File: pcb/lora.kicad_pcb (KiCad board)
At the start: 4 copper layers, 80.5 x 45.1 mm, 82 parts, among them J1 Conn_01x04, J11 Conn_Coaxial, J2 5V, J3 Conn_01x06, J5 Temp, J6 VDD, J7 UART, Q1 AO3401A, Q2 AO3401A, Q3 AO3401A, Q5 AO3401A, SW1 RESET, SW2 PJ, SW3 K3-1296S-E1, U1 ME2108C50M5G, U2 ESP32-WROOM-32D, U3 2460, U4 RFM95W-868S2, U5 SCT2400

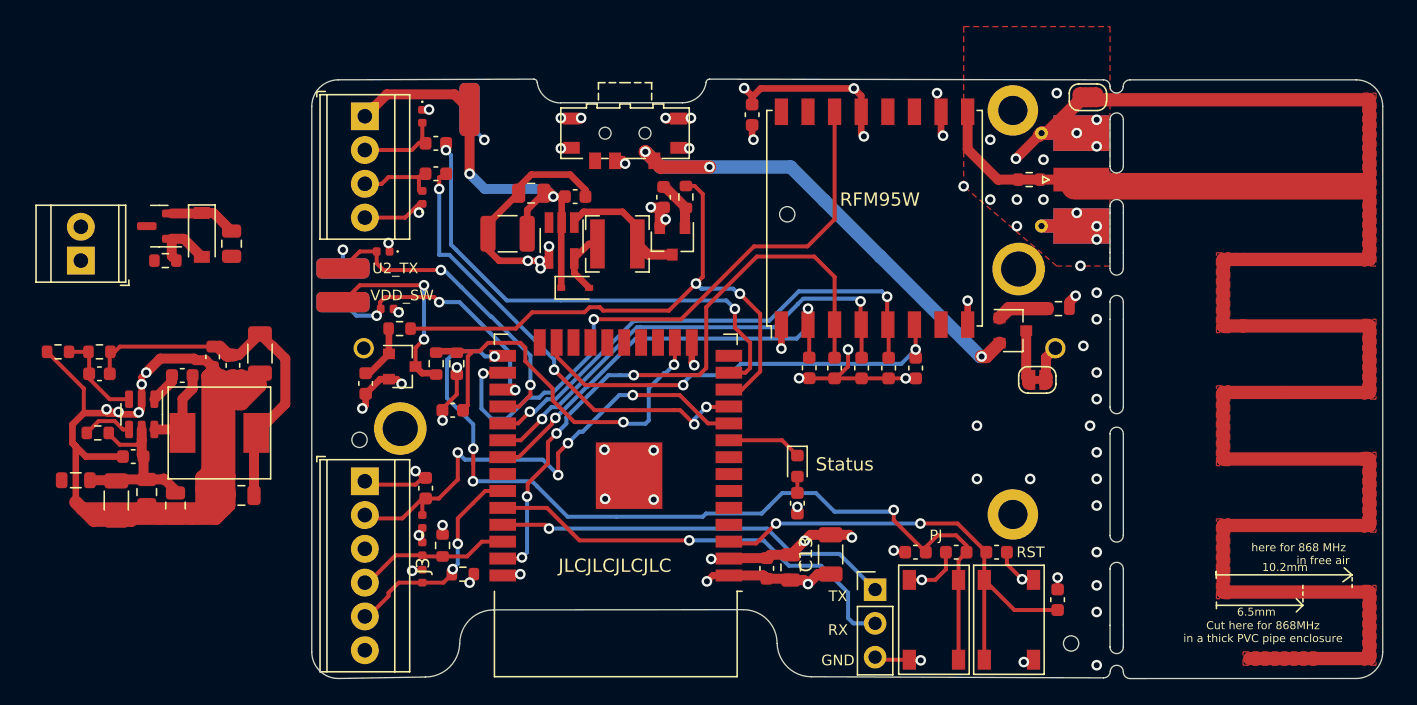
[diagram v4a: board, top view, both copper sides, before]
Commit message: added usb - serial and external power supply
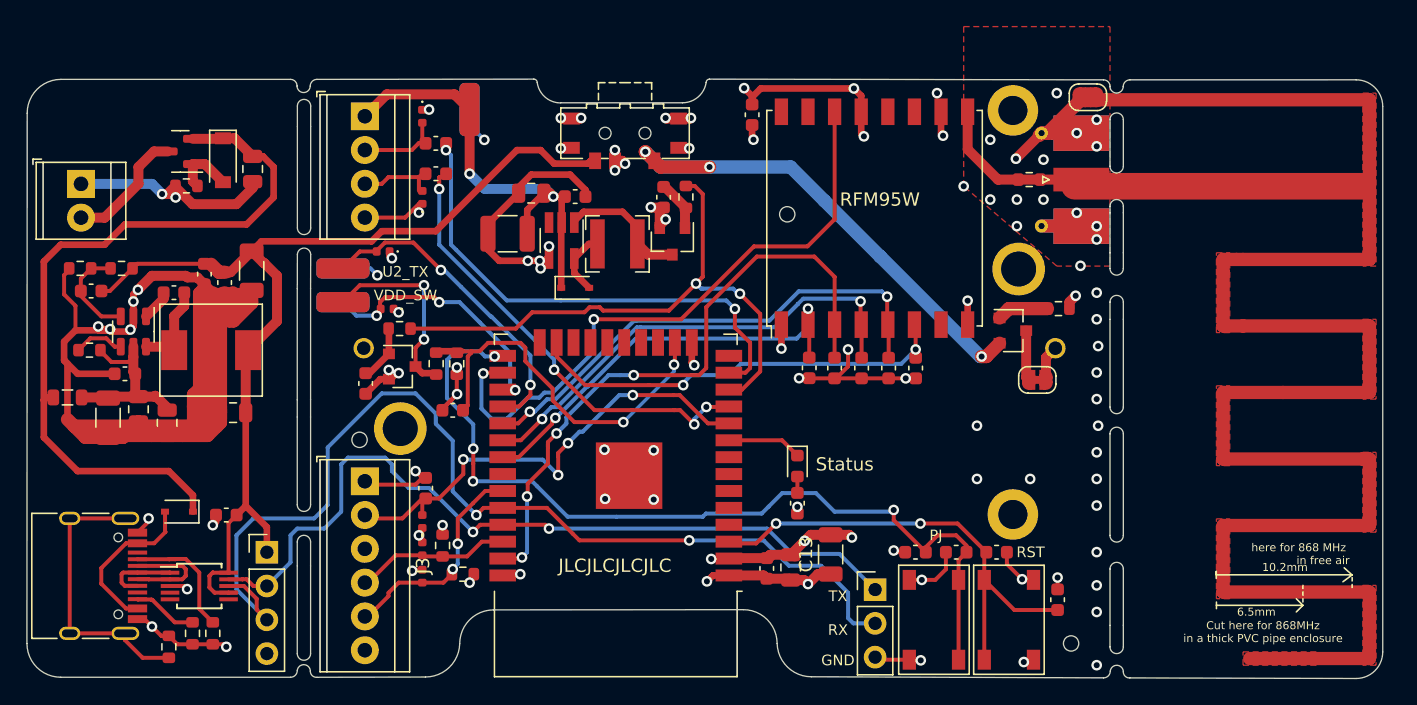
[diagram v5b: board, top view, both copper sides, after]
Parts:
- added C11: 100n, Capacitor_SMD:C_0603_1608Metric, F.Cu at (163.6, 124.7)
- added D11: D_Schottky, Diode_SMD:D_SOD-323, F.Cu at (160.0, 124.5)
- added J4: USB_C_Receptacle_USB2.0, Connector_USB:USB_C_Receptacle_HRO_TYPE-C-31-M-12, F.Cu at (152.9, 129.3)
- added J8: Conn_01x04, Connector_PinHeader_2.54mm:PinHeader_1x04_P2.54mm_Vertical, F.Cu at (166.6, 127.5)
- added R25: 1M, Resistor_SMD:R_0603_1608Metric, F.Cu at (159.3, 134.6)
- added R26: 5.11k, Resistor_SMD:R_0603_1608Metric, F.Cu at (162.6, 133.6)
- added R27: 5.11k, Resistor_SMD:R_0603_1608Metric, F.Cu at (161.0, 133.6)
- added U6: CH340E, Package_SO:MSOP-10_3x3mm_P0.5mm, F.Cu at (161.5, 130.0)
- moved R22 6.49 mm to (152.6, 106.2)
- moved R21 6.49 mm to (155.7, 106.2)
- moved FB1 6.25 mm to (151.6, 115.9)
- moved C14 6.25 mm to (156.0, 114.1)
- moved R18 6.25 mm to (153.3, 112.3)
- moved C10 6.25 mm to (159.1, 117.8)
- moved C16 6.25 mm to (159.6, 108.0)
- moved C17 6.25 mm to (153.4, 107.9)
- moved C18 6.25 mm to (164.1, 117.0)
- moved C19 6.25 mm to (163.4, 107.2)
- moved C20 6.25 mm to (161.9, 106.6)
- moved C21 6.25 mm to (165.5, 106.3)
- moved C4 6.25 mm to (154.7, 117.4)
- moved C8 6.25 mm to (157.0, 116.8)
- moved L3 6.25 mm to (162.4, 112.3)
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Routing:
- net VSUPPLY: track 5.08 -> 56.8 mm
- net 3V3EXT: track 27.4 -> 77.3 mm
- net PRG_RX: track 32.7 -> 78.1 mm, vias 1 -> 2
- net PRG_TX: track 30.0 -> 60.9 mm, vias 1 -> 2
- net GND: track 205.3 -> 235.1 mm, vias 75 -> 82
- net Net-(J4-PadS1): track 0.00 -> 21.4 mm
- net Net-(J4-PadA4): track 0.00 -> 12.2 mm
- net Net-(J4-PadA5): track 0.00 -> 9.74 mm
- net VSUPPLY_IN: track 0.00 -> 9.34 mm
- net Net-(J4-PadA7): track 0.00 -> 7.99 mm
- net Net-(J4-PadA6): track 0.00 -> 5.63 mm
- net Net-(J4-PadB5): track 0.00 -> 4.86 mm
- net ONEWIRE1_DATA: track 37.3 -> 36.2 mm
- net VDD_SENSE: track 31.2 -> 30.2 mm
- net VDD: track 55.7 -> 56.6 mm, vias 20 -> 22
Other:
- board size 80.5 x 45.1 mm -> 101.9 x 45.1 mm

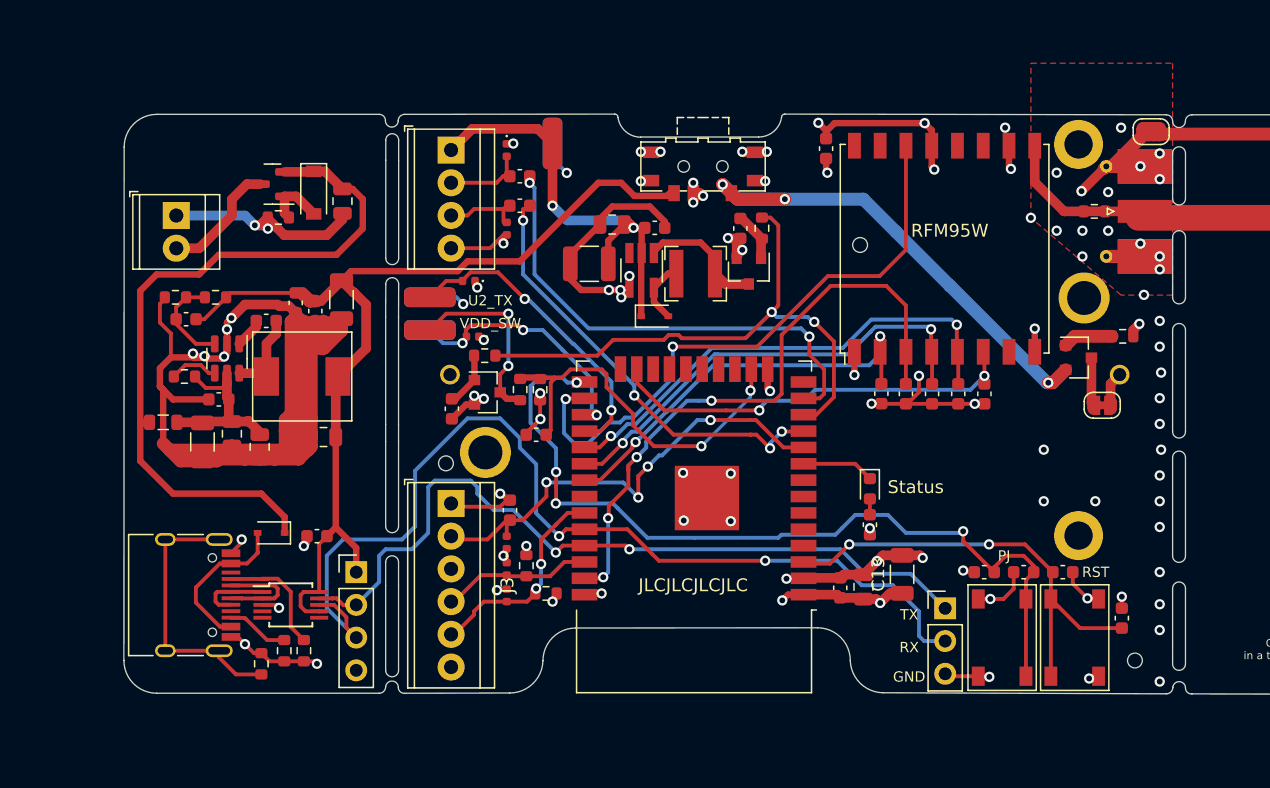
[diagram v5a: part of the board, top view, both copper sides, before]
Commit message: fixed DRC errors
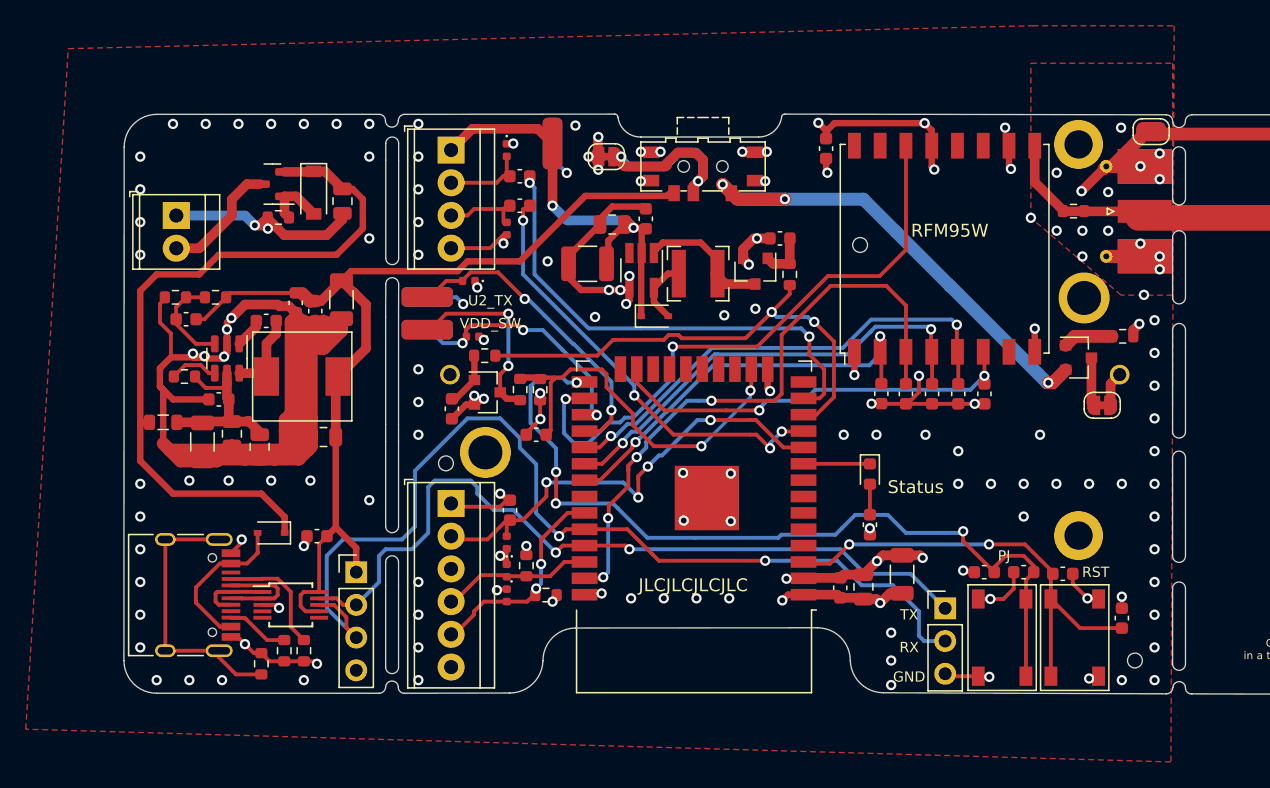
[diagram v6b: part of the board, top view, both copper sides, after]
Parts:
- added JP3: ISense, Jumper:SolderJumper-2_P1.3mm_Bridged_RoundedPad1.0x1.5mm, F.Cu at (186.0, 95.2)
- moved R12 4.19 mm to (200.3, 104.4), turned to 90 degrees
- moved R11 3.17 mm to (199.5, 101.6), turned to 0 degrees
- moved L2 1.62 mm to (222.3, 99.5)
- moved D1 1.14 mm to (206.5, 119.9)
- moved C23 0.99 mm to (189.1, 100.1), turned to -90 degrees
- moved Q3 0.51 mm to (197.6, 104.1)
- moved J7 0.20 mm to (172.1, 107.4)
- moved L1 0.19 mm to (193.2, 104.3)
- moved C3 0.14 mm to (184.6, 103.6)
- moved C5 0.13 mm to (221.5, 127.6)
- moved R15 0.13 mm to (181.4, 129.3)
- moved D5 0.13 mm to (178.3, 127.4)
- renumbered C13 to Ce
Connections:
- SW3 pad 2: VDD -> Net-(SW3-Pad2)
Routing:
- net Net-(SW3-Pad2): track 0.00 -> 20.6 mm, vias 0 -> 2
- net POWER_EN: track 44.5 -> 38.8 mm
- net 3V3EXT: track 77.3 -> 75.8 mm
- net Net-(D1-Pad2): track 1.23 -> 2.37 mm
- net VDD: track 56.6 -> 57.4 mm
- net unconnected-(U2-Pad7): track 0.81 -> 0.00 mm
- net unconnected-(U2-Pad6): track 0.81 -> 0.00 mm
- net unconnected-(U2-Pad4): track 0.81 -> 0.00 mm
- net EXT_ADC_SENSE2: track 34.8 -> 34.3 mm
- net 5V_EN: track 9.86 -> 10.4 mm
- net GND: track 235.1 -> 235.0 mm, vias 82 -> 143
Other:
- outline, holes or cut-outs redrawn
